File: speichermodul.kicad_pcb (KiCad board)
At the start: 2 copper layers, 100 x 160 mm, 66 parts, among them IC1 6116, P1 CONN_3X2, P2 CONN_01X01, P3 CONN_01X01, P4 CONN_01X01, P5 CONN_01X01, P6 CONN_01X01, P7 CONN_01X01, P8 CONN_02X10, P9 CONN_02X10, SW1 SW_PUSH, SW2 SW_PUSH, U1 7400, U2 74LS08, U3 74LS08, U4 74LS14, U5 74LS540, U6 74LS540

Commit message: Pcb layout kabelverlegt
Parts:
- moved P8 26.6 mm to (115.6, 175.3), turned to 180 degrees
- moved P4 18.0 mm to (34.3, 174.0)
- moved SW2 16.5 mm to (40.6, 156.2), turned to 180 degrees
- moved R10 11.5 mm to (66.0, 47.0)
- moved R13 11.5 mm to (71.1, 47.0)
- moved R14 11.5 mm to (88.9, 36.8)
- moved R15 11.5 mm to (94.0, 47.0)
- moved R11 11.5 mm to (82.5, 47.0)
- moved R12 11.5 mm to (55.9, 47.0)
- moved R4 11.5 mm to (61.0, 47.0)
- moved R9 11.5 mm to (77.5, 47.0)
- moved U6 9.41 mm to (64.8, 160.0)
- moved D13 9.25 mm to (67.3, 127.0), turned to 90 degrees
- moved D14 9.25 mm to (72.4, 127.0), turned to 90 degrees
- moved D11 9.25 mm to (57.1, 127.0), turned to 90 degrees
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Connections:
- D10 pad 1: GND -> Net-(D10-Pad1)
- D10 pad 2: Net-(D10-Pad2) -> VCC
- D11 pad 1: GND -> Net-(D11-Pad1)
- D11 pad 2: Net-(D11-Pad2) -> VCC
- D12 pad 1: GND -> Net-(D12-Pad1)
- D12 pad 2: Net-(D12-Pad2) -> VCC
- D13 pad 1: GND -> Net-(D13-Pad1)
- D13 pad 2: Net-(D13-Pad2) -> VCC
- D14 pad 1: GND -> Net-(D14-Pad1)
- D14 pad 2: Net-(D14-Pad2) -> VCC
- D15 pad 1: GND -> Net-(D15-Pad1)
- D15 pad 2: Net-(D15-Pad2) -> VCC
- D16 pad 1: GND -> Net-(D16-Pad1)
- D16 pad 2: Net-(D16-Pad2) -> VCC
- D17 pad 1: GND -> Net-(D17-Pad1)
- D17 pad 2: Net-(D17-Pad2) -> VCC
- D18 pad 1: GND -> Net-(D18-Pad1)
- D18 pad 2: Net-(D18-Pad2) -> VCC
- D3 pad 1: GND -> Net-(D3-Pad1)
- D3 pad 2: Net-(D3-Pad2) -> VCC
- D4 pad 1: GND -> Net-(D4-Pad1)
- D4 pad 2: Net-(D4-Pad2) -> VCC
- D5 pad 1: GND -> Net-(D5-Pad1)
- D5 pad 2: Net-(D5-Pad2) -> VCC
- D6 pad 1: GND -> Net-(D6-Pad1)
- D6 pad 2: Net-(D6-Pad2) -> VCC
- D7 pad 1: GND -> Net-(D7-Pad1)
- D7 pad 2: Net-(D7-Pad2) -> VCC
- D8 pad 1: GND -> Net-(D8-Pad1)
- D8 pad 2: Net-(D8-Pad2) -> VCC
- D9 pad 1: GND -> Net-(D9-Pad1)
- D9 pad 2: Net-(D9-Pad2) -> VCC
- R10 pad 1: Net-(D5-Pad2) -> Net-(D8-Pad1)
- R11 pad 1: Net-(D6-Pad2) -> Net-(D7-Pad1)
- R12 pad 1: Net-(D7-Pad2) -> Net-(D6-Pad1)
- R13 pad 1: Net-(D8-Pad2) -> Net-(D5-Pad1)
- R14 pad 1: Net-(D9-Pad2) -> Net-(D4-Pad1)
- R15 pad 1: Net-(D10-Pad2) -> Net-(D3-Pad1)
- R16 pad 1: Net-(D11-Pad2) -> Net-(D18-Pad1)
- R17 pad 1: Net-(D12-Pad2) -> Net-(D17-Pad1)
- R18 pad 1: Net-(D13-Pad2) -> Net-(D16-Pad1)
- R19 pad 1: Net-(D14-Pad2) -> Net-(D15-Pad1)
- R20 pad 1: Net-(D15-Pad2) -> Net-(D14-Pad1)
- R21 pad 1: Net-(D16-Pad2) -> Net-(D13-Pad1)
- R22 pad 1: Net-(D17-Pad2) -> Net-(D12-Pad1)
- R23 pad 1: Net-(D18-Pad2) -> Net-(D11-Pad1)
- R4 pad 1: Net-(D3-Pad2) -> Net-(D10-Pad1)
- R9 pad 1: Net-(D4-Pad2) -> Net-(D9-Pad1)
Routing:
- net GND: track 4.00 -> 180.3 mm
- net VCC: track 0.00 -> 77.6 mm
- net /D7: track 0.00 -> 72.8 mm
- net /A0: track 0.00 -> 72.3 mm, vias 0 -> 2
- net /A1: track 0.00 -> 66.8 mm, vias 0 -> 2
- net /A2: track 0.00 -> 61.1 mm, vias 0 -> 2
- net /A3: track 0.00 -> 55.5 mm, vias 0 -> 2
- net /A4: track 0.00 -> 49.9 mm, vias 0 -> 2
- net /A5: track 0.00 -> 44.4 mm, vias 0 -> 2
- net /A6: track 0.00 -> 38.6 mm, vias 0 -> 2
- net /A7: track 0.00 -> 31.8 mm
- net Net-(D1-Pad1): track 0.00 -> 22.6 mm
- net Net-(D9-Pad2): track 19.9 -> 0.00 mm
- net Net-(R16-Pad2): track 0.00 -> 17.7 mm
- net Net-(R17-Pad2): track 0.00 -> 15.9 mm
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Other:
- net class Default: trace_width 0.25 -> 1

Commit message: Switch Layer
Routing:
- net /A2: track 61.1 -> 62.3 mm

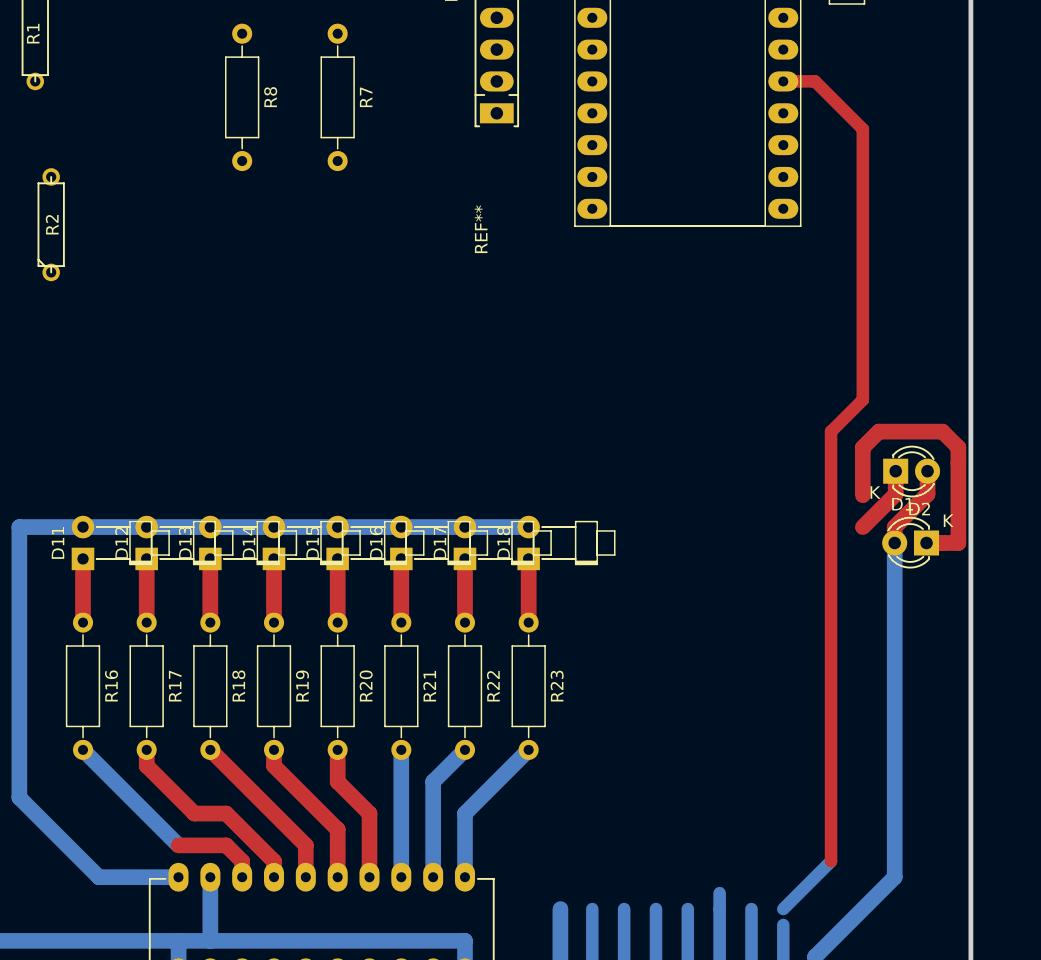
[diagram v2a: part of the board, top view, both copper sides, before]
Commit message: changed cupper front layer to bottom layer
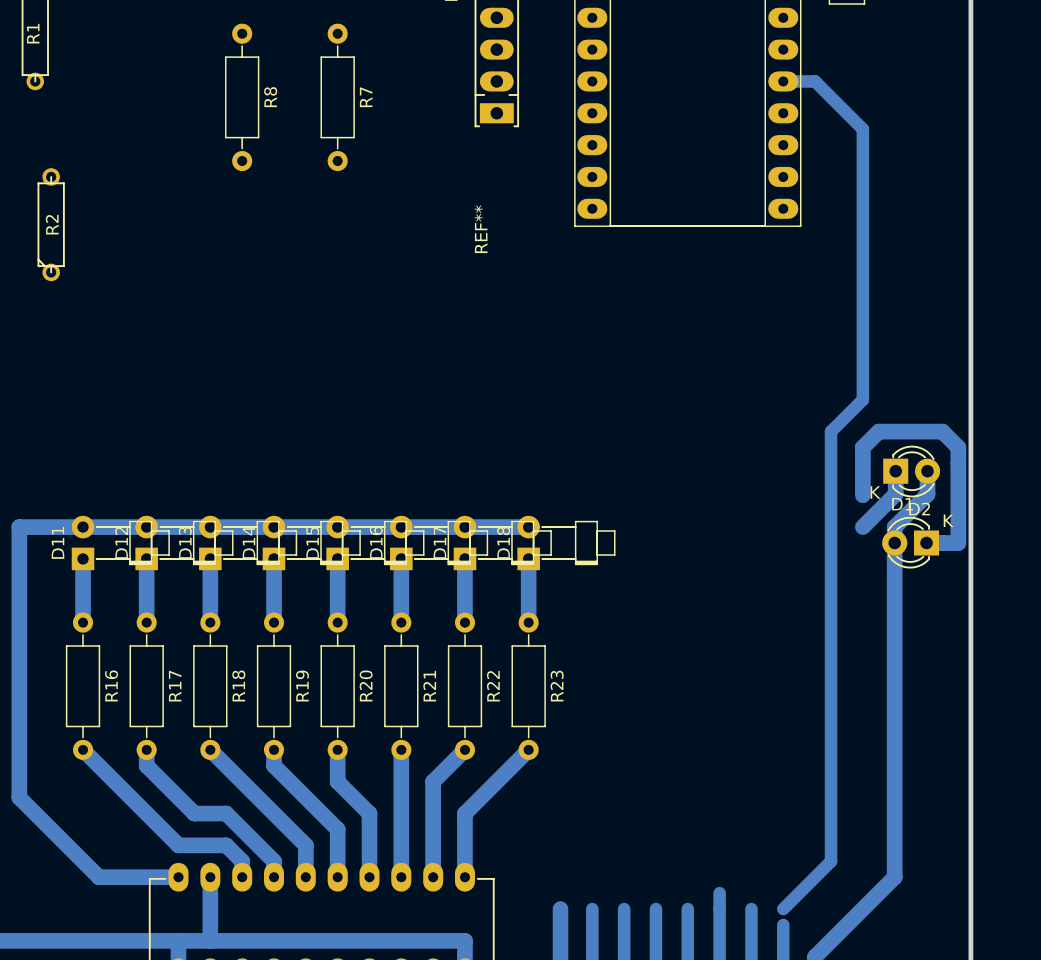
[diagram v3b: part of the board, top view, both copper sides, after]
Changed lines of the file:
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@@
   (segment (start 52.07 146.05) (end 58.42 152.4) (width 1.25) (layer B.Cu) (net 1))
   (segment (start 92.71 124.46) (end 57.15 124.46) (width 1.25) (layer B.Cu) (net 1) (status C00000))
-  (segment (start 113.03 88.9) (end 115.57 88.9) (width 1) (layer F.Cu) (net 9) (status 400000))
+  (segment (start 113.03 88.9) (end 115.57 88.9) (width 1) (layer B.Cu) (net 9) (status 400000))
   (segment (start 116.84 151.13) (end 113.03 154.94) (width 1) (layer B.Cu) (net 9))
-  (segment (start 116.84 116.84) (end 116.84 151.13) (width 1) (layer F.Cu) (net 9))
-  (segment (start 119.38 114.3) (end 116.84 116.84) (width 1) (layer F.Cu) (net 9))
-  (segment (start 119.38 92.71) (end 119.38 114.3) (width 1) (layer F.Cu) (net 9))
-  (segment (start 115.57 88.9) (end 119.38 92.71) (width 1) (layer F.Cu) (net 9))
+  (segment (start 116.84 116.84) (end 116.84 151.13) (width 1) (layer B.Cu) (net 9))
+  (segment (start 119.38 114.3) (end 116.84 116.84) (width 1) (layer B.Cu) (net 9))
+  (segment (start 119.38 92.71) (end 119.38 114.3) (width 1) (layer B.Cu) (net 9))
+  (segment (start 115.57 88.9) (end 119.38 92.71) (width 1) (layer B.Cu) (net 9))
   (segment (start 64.77 157.48) (end 43.18 157.48) (width 1.25) (layer B.Cu) (net 10))
   (segment (start 41.91 157.48) (end 40.64 156.21) (width 1.25) (layer B.Cu) (net 10) (status 800000))
@@
   (segment (start 64.77 162.56) (end 77.47 175.26) (width 1) (layer B.Cu) (net 10))
   (segment (start 77.47 175.26) (end 92.71 175.26) (width 1.25) (layer B.Cu) (net 10) (status 800000))
-  (segment (start 121.92 125.73) (end 121.92 124.46) (width 1.25) (layer F.Cu) (net 10) (status 400000))
-  (segment (start 124.54 121.84) (end 124.54 120) (width 1.25) (layer F.Cu) (net 10) (status 800000))
-  (segment (start 121.92 124.46) (end 124.54 121.84) (width 1.25) (layer F.Cu) (net 10))
+  (segment (start 121.92 125.73) (end 121.92 124.46) (width 1.25) (layer B.Cu) (net 10) (status 400000))
+  (segment (start 124.54 121.84) (end 124.54 120) (width 1.25) (layer B.Cu) (net 10) (status 800000))
+  (segment (start 121.92 124.46) (end 124.54 121.84) (width 1.25) (layer B.Cu) (net 10))
   (segment (start 115.57 175.26) (end 115.57 158.75) (width 1.25) (layer B.Cu) (net 10) (status 400000))
   (segment (start 121.92 152.4) (end 121.92 125.73) (width 1.25) (layer B.Cu) (net 10) (status 800000))
@@
   (segment (start 87.63 157.48) (end 87.63 160.02) (width 1.25) (layer B.Cu) (net 10) (status 800000))
   (segment (start 67.31 157.48) (end 87.63 157.48) (width 1.25) (layer B.Cu) (net 10))
-  (segment (start 69.85 152.4) (end 69.85 151.13) (width 1.25) (layer F.Cu) (net 19) (status 400000))
+  (segment (start 69.85 152.4) (end 69.85 151.13) (width 1.25) (layer B.Cu) (net 19) (status 400000))
   (segment (start 64.77 149.86) (end 57.15 142.24) (width 1.25) (layer B.Cu) (net 19) (status 800000))
-  (segment (start 68.58 149.86) (end 64.77 149.86) (width 1.25) (layer F.Cu) (net 19))
-  (segment (start 69.85 151.13) (end 68.58 149.86) (width 1.25) (layer F.Cu) (net 19))
-  (segment (start 72.39 152.4) (end 72.39 151.13) (width 1.25) (layer F.Cu) (net 20) (status 400000))
-  (segment (start 62.23 143.51) (end 62.23 142.24) (width 1.25) (layer F.Cu) (net 20) (status 800000))
-  (segment (start 66.04 147.32) (end 62.23 143.51) (width 1.25) (layer F.Cu) (net 20))
-  (segment (start 68.58 147.32) (end 66.04 147.32) (width 1.25) (layer F.Cu) (net 20))
-  (segment (start 72.39 151.13) (end 68.58 147.32) (width 1.25) (layer F.Cu) (net 20))
-  (segment (start 74.93 152.4) (end 74.93 149.86) (width 1.25) (layer F.Cu) (net 21) (status 400000))
-  (segment (start 74.93 149.86) (end 67.31 142.24) (width 1.25) (layer F.Cu) (net 21) (status 800000))
-  (segment (start 77.47 152.4) (end 77.47 148.59) (width 1.25) (layer F.Cu) (net 22) (status 400000))
-  (segment (start 72.39 143.51) (end 72.39 142.24) (width 1.25) (layer F.Cu) (net 22) (status 800000))
-  (segment (start 77.47 148.59) (end 72.39 143.51) (width 1.25) (layer F.Cu) (net 22))
-  (segment (start 80.01 152.4) (end 80.01 147.32) (width 1.25) (layer F.Cu) (net 23) (status 400000))
-  (segment (start 77.47 144.78) (end 77.47 142.24) (width 1.25) (layer F.Cu) (net 23) (status 800000))
-  (segment (start 80.01 147.32) (end 77.47 144.78) (width 1.25) (layer F.Cu) (net 23))
+  (segment (start 68.58 149.86) (end 64.77 149.86) (width 1.25) (layer B.Cu) (net 19))
+  (segment (start 69.85 151.13) (end 68.58 149.86) (width 1.25) (layer B.Cu) (net 19))
+  (segment (start 72.39 152.4) (end 72.39 151.13) (width 1.25) (layer B.Cu) (net 20) (status 400000))
+  (segment (start 62.23 143.51) (end 62.23 142.24) (width 1.25) (layer B.Cu) (net 20) (status 800000))
+  (segment (start 66.04 147.32) (end 62.23 143.51) (width 1.25) (layer B.Cu) (net 20))
+  (segment (start 68.58 147.32) (end 66.04 147.32) (width 1.25) (layer B.Cu) (net 20))
+  (segment (start 72.39 151.13) (end 68.58 147.32) (width 1.25) (layer B.Cu) (net 20))
+  (segment (start 74.93 152.4) (end 74.93 149.86) (width 1.25) (layer B.Cu) (net 21) (status 400000))
+  (segment (start 74.93 149.86) (end 67.31 142.24) (width 1.25) (layer B.Cu) (net 21) (status 800000))
+  (segment (start 77.47 152.4) (end 77.47 148.59) (width 1.25) (layer B.Cu) (net 22) (status 400000))
+  (segment (start 72.39 143.51) (end 72.39 142.24) (width 1.25) (layer B.Cu) (net 22) (status 800000))
+  (segment (start 77.47 148.59) (end 72.39 143.51) (width 1.25) (layer B.Cu) (net 22))
+  (segment (start 80.01 152.4) (end 80.01 147.32) (width 1.25) (layer B.Cu) (net 23) (status 400000))
+  (segment (start 77.47 144.78) (end 77.47 142.24) (width 1.25) (layer B.Cu) (net 23) (status 800000))
+  (segment (start 80.01 147.32) (end 77.47 144.78) (width 1.25) (layer B.Cu) (net 23))
   (segment (start 82.55 152.4) (end 82.55 142.24) (width 1.25) (layer B.Cu) (net 24) (status C00000))
   (segment (start 85.09 152.4) (end 85.09 144.78) (width 1.25) (layer B.Cu) (net 25) (status 400000))
@@
   (segment (start 113.03 171.45) (end 113.03 156.21) (width 1) (layer B.Cu) (net 34))
   (segment (start 113.03 175.26) (end 113.03 173.99) (width 1) (layer B.Cu) (net 34) (status 400000))
-  (segment (start 124.46 125.73) (end 125.73 125.73) (width 1.25) (layer F.Cu) (net 35) (status 400000))
-  (segment (start 119.38 118.11) (end 119.38 121.92) (width 1.25) (layer F.Cu) (net 35))
-  (segment (start 120.65 116.84) (end 119.38 118.11) (width 1.25) (layer F.Cu) (net 35))
-  (segment (start 125.73 116.84) (end 120.65 116.84) (width 1.25) (layer F.Cu) (net 35))
-  (segment (start 127 118.11) (end 125.73 116.84) (width 1.25) (layer F.Cu) (net 35))
-  (segment (start 127 119.38) (end 127 118.11) (width 1.25) (layer F.Cu) (net 35))
-  (segment (start 127 125.73) (end 127 119.38) (width 1.25) (layer F.Cu) (net 35))
-  (segment (start 125.73 125.73) (end 127 125.73) (width 1.25) (layer F.Cu) (net 35))
-  (segment (start 122 120) (end 122 121.84) (width 1.25) (layer F.Cu) (net 36) (status 400000))
-  (segment (start 122 121.84) (end 119.38 124.46) (width 1.25) (layer F.Cu) (net 36))
-  (segment (start 57.15 132.08) (end 57.15 127) (width 1.25) (layer F.Cu) (net 77) (status C00000))
-  (segment (start 62.23 132.08) (end 62.23 127) (width 1.25) (layer F.Cu) (net 76) (status C00000))
-  (segment (start 67.31 132.08) (end 67.31 127) (width 1.25) (layer F.Cu) (net 75) (status C00000))
-  (segment (start 72.39 132.08) (end 72.39 127) (width 1.25) (layer F.Cu) (net 74) (status C00000))
-  (segment (start 77.47 132.08) (end 77.47 127) (width 1.25) (layer F.Cu) (net 73) (status C00000))
-  (segment (start 82.55 132.08) (end 82.55 127) (width 1.25) (layer F.Cu) (net 72) (status C00000))
-  (segment (start 87.63 132.08) (end 87.63 127) (width 1.25) (layer F.Cu) (net 71) (status C00000))
-  (segment (start 92.71 132.08) (end 92.71 127) (width 1.25) (layer F.Cu) (net 70) (status C00000))
+  (segment (start 124.46 125.73) (end 125.73 125.73) (width 1.25) (layer B.Cu) (net 35) (status 400000))
+  (segment (start 119.38 118.11) (end 119.38 121.92) (width 1.25) (layer B.Cu) (net 35))
+  (segment (start 120.65 116.84) (end 119.38 118.11) (width 1.25) (layer B.Cu) (net 35))
+  (segment (start 125.73 116.84) (end 120.65 116.84) (width 1.25) (layer B.Cu) (net 35))
+  (segment (start 127 118.11) (end 125.73 116.84) (width 1.25) (layer B.Cu) (net 35))
+  (segment (start 127 119.38) (end 127 118.11) (width 1.25) (layer B.Cu) (net 35))
+  (segment (start 127 125.73) (end 127 119.38) (width 1.25) (layer B.Cu) (net 35))
+  (segment (start 125.73 125.73) (end 127 125.73) (width 1.25) (layer B.Cu) (net 35))
+  (segment (start 122 120) (end 122 121.84) (width 1.25) (layer B.Cu) (net 36) (status 400000))
+  (segment (start 122 121.84) (end 119.38 124.46) (width 1.25) (layer B.Cu) (net 36))
+  (segment (start 57.15 132.08) (end 57.15 127) (width 1.25) (layer B.Cu) (net 77) (status C00000))
+  (segment (start 62.23 132.08) (end 62.23 127) (width 1.25) (layer B.Cu) (net 76) (status C00000))
+  (segment (start 67.31 132.08) (end 67.31 127) (width 1.25) (layer B.Cu) (net 75) (status C00000))
+  (segment (start 72.39 132.08) (end 72.39 127) (width 1.25) (layer B.Cu) (net 74) (status C00000))
+  (segment (start 77.47 132.08) (end 77.47 127) (width 1.25) (layer B.Cu) (net 73) (status C00000))
+  (segment (start 82.55 132.08) (end 82.55 127) (width 1.25) (layer B.Cu) (net 72) (status C00000))
+  (segment (start 87.63 132.08) (end 87.63 127) (width 1.25) (layer B.Cu) (net 71) (status C00000))
+  (segment (start 92.71 132.08) (end 92.71 127) (width 1.25) (layer B.Cu) (net 70) (status C00000))
 )
